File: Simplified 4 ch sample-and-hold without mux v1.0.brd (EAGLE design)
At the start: 19.1 x 10.8 mm, 8 parts, among them IC5 TL074JT

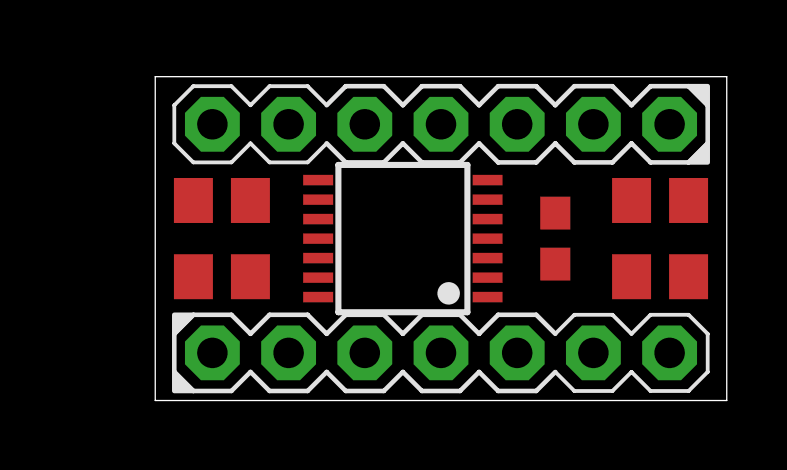
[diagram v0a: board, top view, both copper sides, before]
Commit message: Almost completed simplified 4ch s & h
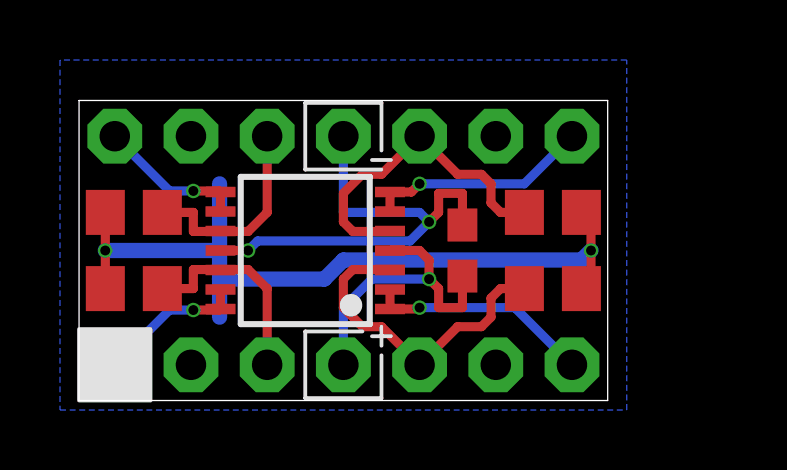
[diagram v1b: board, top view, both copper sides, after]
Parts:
- removed U$2, U$3: MA07-1JC, joakim:MA07-1J
- added 1-7, 8-14: MA07-1JN, joakim:MA07N-1J
- moved C28 3.59 mm to (15.8, 6.27), turned to 180 degrees
- moved C29 3.59 mm to (15.8, 3.73)
- moved IC5 3.28 mm to (7.54, 5.00)
- moved C31 3.12 mm to (12.8, 5.00)
- moved C26 2.96 mm to (1.83, 3.73)
- moved C27 2.96 mm to (1.83, 6.27)
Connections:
- net +15V: now also 1-7.4
- net -15V: now also 8-14.4
- net AGND: now also 1-7.2
- net IN1: now also 1-7.3, C26.2, IC5.12; no longer C29.2, IC5.3
- net IN2: now also 1-7.5, C29.2, IC5.3; no longer C26.2, IC5.12
- net IN3: now also 8-14.3, C28.2, IC5.5; no longer C27.2, IC5.10
- net IN4: now also 8-14.5, C27.2, IC5.10; no longer C28.2, IC5.5
- net OUT1: now also 1-7.1, IC5.13, IC5.14; no longer IC5.1, IC5.2
- net OUT2: now also 1-7.7, IC5.1, IC5.2; no longer IC5.13, IC5.14
- net OUT3: now also 8-14.1, IC5.6, IC5.7; no longer IC5.8, IC5.9
- net OUT4: now also 8-14.7, IC5.8, IC5.9; no longer IC5.6, IC5.7
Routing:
- net AGND: track 0.00 -> 26.4 mm, vias 0 -> 2
- net -15V: track 0.00 -> 15.8 mm, vias 0 -> 2
- net IN2: track 0.00 -> 10.9 mm
- net IN3: track 0.00 -> 10.9 mm
- net +15V: track 0.00 -> 10.2 mm, vias 0 -> 1
- net OUT2: track 0.00 -> 7.52 mm, vias 0 -> 1
- net OUT3: track 0.00 -> 7.49 mm, vias 0 -> 1
- net IN1: track 0.00 -> 6.95 mm
- net IN4: track 0.00 -> 6.95 mm
- net OUT4: track 0.00 -> 4.95 mm, vias 0 -> 1
- net OUT1: track 0.00 -> 4.95 mm, vias 0 -> 1
- added copper zone on layer 16, net AGND
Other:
- board size 19.1 x 10.8 mm -> 17.6 x 10 mm
- board text added: "4VOB"
- board text added: "S&H v1.0"
